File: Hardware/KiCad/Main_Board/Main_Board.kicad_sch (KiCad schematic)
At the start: 0 parts

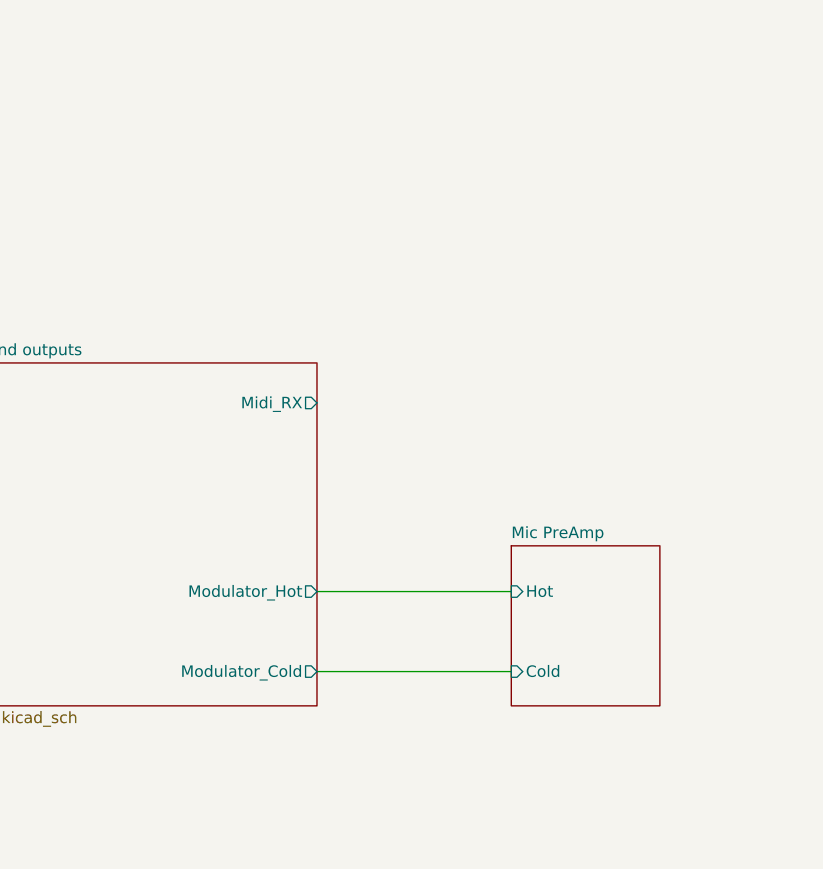
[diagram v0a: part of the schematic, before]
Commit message: Reorganised+rename Main_Board project
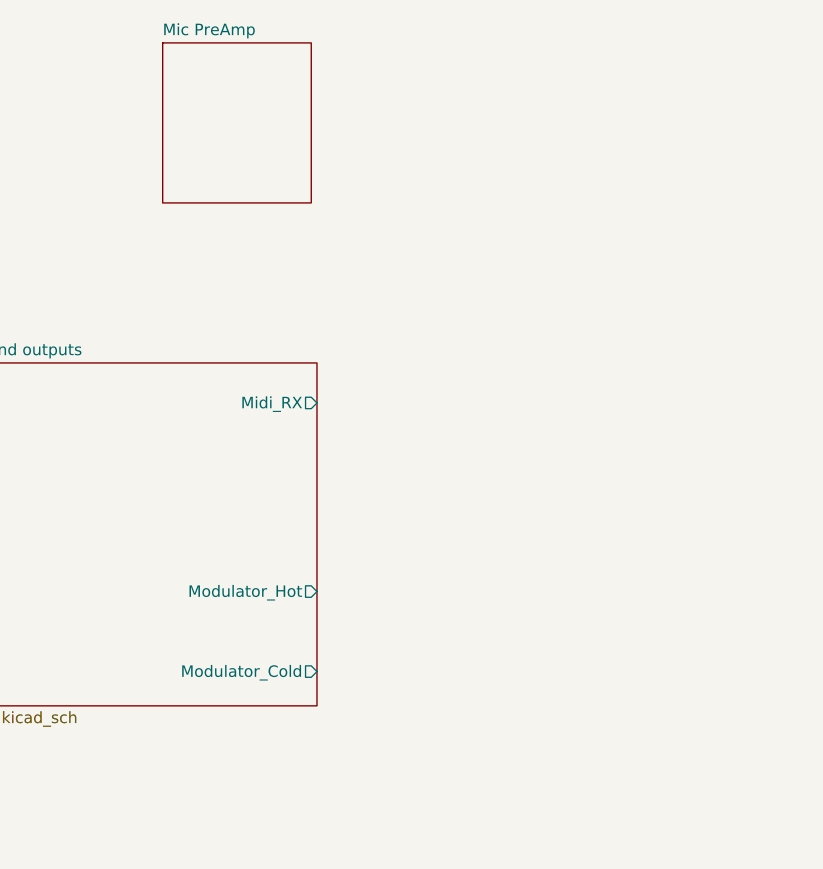
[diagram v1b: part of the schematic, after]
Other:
- sheet Mic PreAmp ports: added none; removed Cold, Hot
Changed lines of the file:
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@@
 		(comment 1 "Tim Wannet")
-	)
-	(wire
-		(pts
-			(xy 67.31 101.6) (xy 88.9 101.6)
-		)
-		(stroke
-			(width 0)
-			(type default)
-		)
-	)
-	(wire
-		(pts
-			(xy 67.31 110.49) (xy 88.9 110.49)
-		)
-		(stroke
-			(width 0)
-			(type default)
-		)
 	)
 	(sheet
@@
 		)
 		(instances
-			(project "Hardware"
+			(project "Main_Board"
 				(path "/e827c80a-ca8d-4d24-8db6-878b575a1aed"
 					(page "3")
@@
 		)
 		(instances
-			(project "Hardware"
+			(project "Main_Board"
 				(path "/e827c80a-ca8d-4d24-8db6-878b575a1aed"
 					(page "5")
@@
 		)
 		(instances
-			(project "Hardware"
+			(project "Main_Board"
 				(path "/e827c80a-ca8d-4d24-8db6-878b575a1aed"
 					(page "2")
@@
 	)
 	(sheet
-		(at 88.9 96.52)
+		(at 50.165 40.64)
 		(size 16.51 17.78)
 		(exclude_from_sim no)
@@
 		)
 		(property "Sheetname" "Mic PreAmp"
-			(at 88.9 95.8084 0)
+			(at 50.165 39.9284 0)
 			(effects
 				(font
@@
 		)
 		(property "Sheetfile" "PreAmp.kicad_sch"
-			(at 88.9 114.8846 0)
+			(at 50.165 59.0046 0)
 			(effects
 				(font
@@
 			)
 		)
-		(pin "Hot" input
-			(at 88.9 101.6 180)
-			(effects
-				(font
-					(size 1.27 1.27)
-				)
-				(justify left)
-			)
-		)
-		(pin "Cold" input
-			(at 88.9 110.49 180)
-			(effects
-				(font
-					(size 1.27 1.27)
-				)
-				(justify left)
-			)
-		)
 		(instances
-			(project "Hardware"
+			(project "Main_Board"
 				(path "/e827c80a-ca8d-4d24-8db6-878b575a1aed"
 					(page "4")

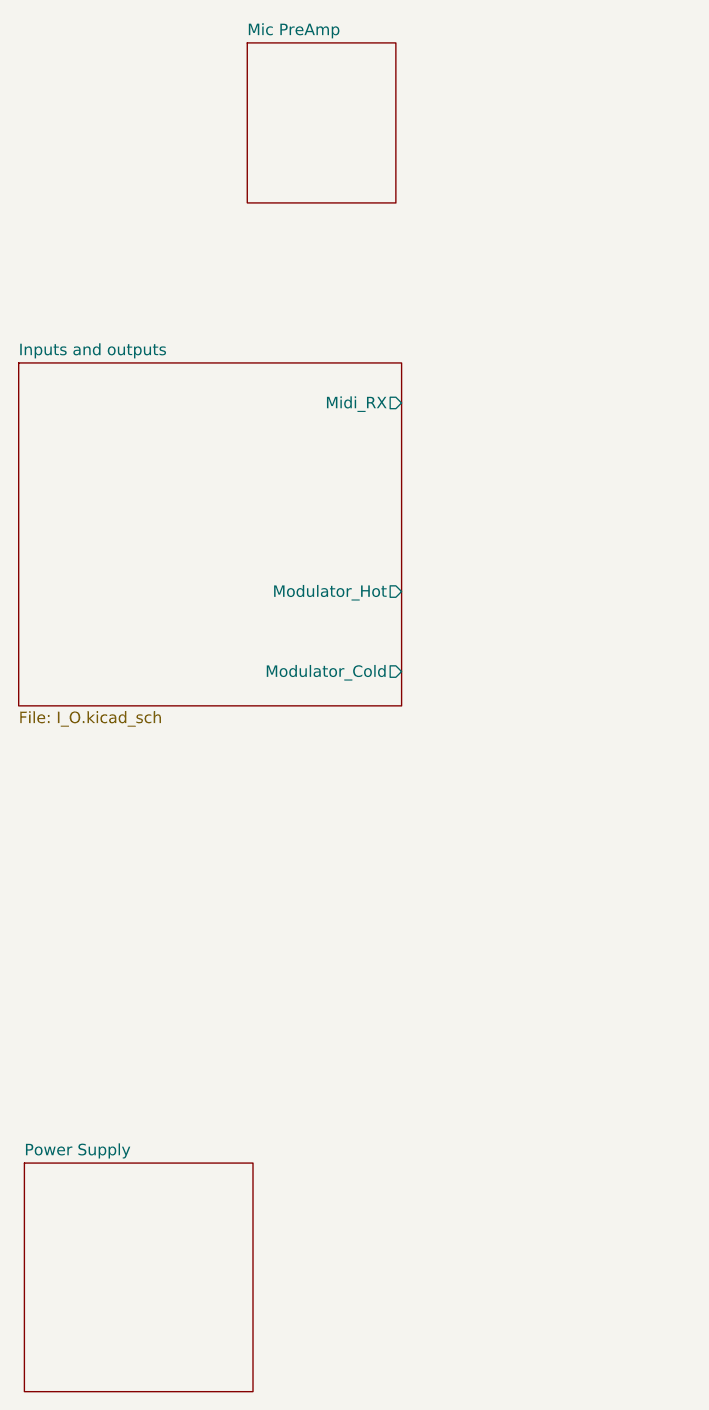
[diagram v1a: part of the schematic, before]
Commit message: Created Female header connections for MCU
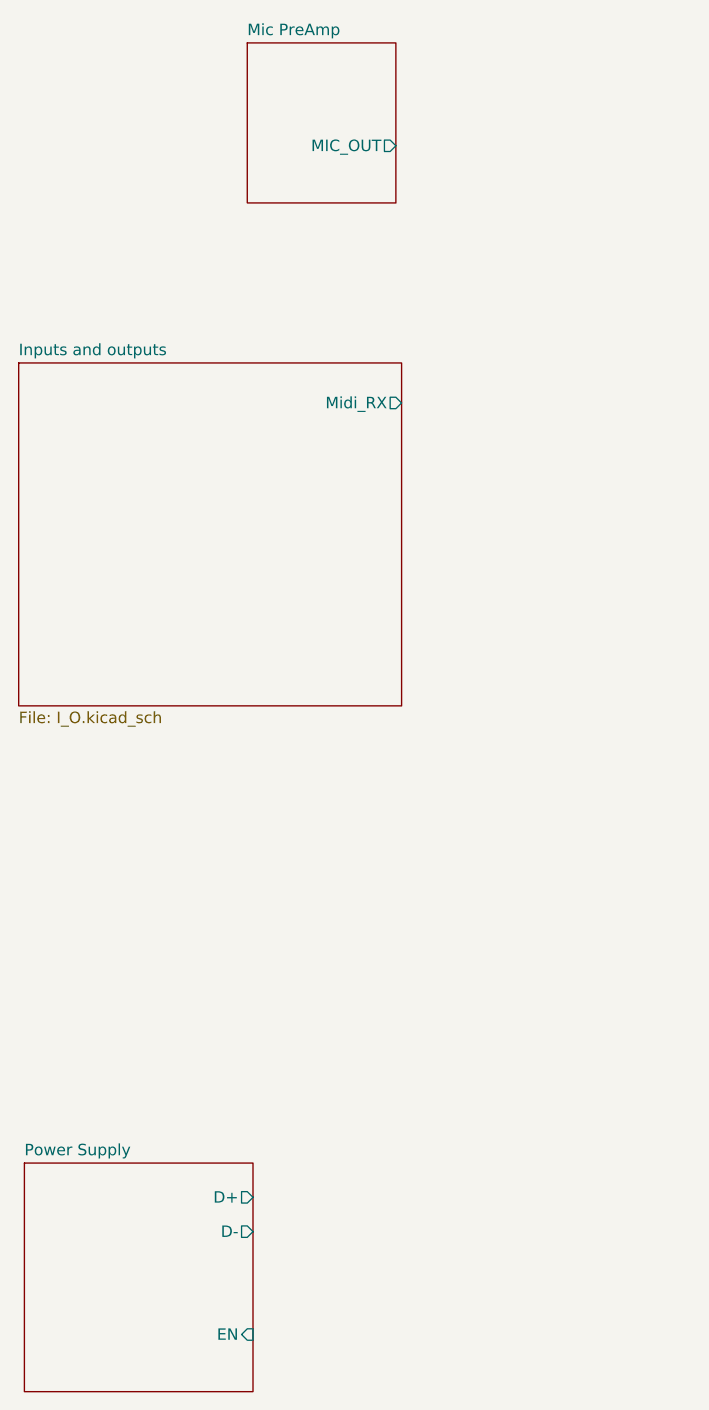
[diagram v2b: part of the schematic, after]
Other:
- sheet Inputs and outputs ports: added none; removed Modulator_Cold, Modulator_Hot
- sheet Mic PreAmp ports: added MIC_OUT; removed none
- sheet Power Supply ports: added D+, D-, EN; removed none
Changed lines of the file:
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@@
-			)
-		)
-		(pin "Modulator_Cold" output
-			(at 67.31 110.49 0)
-			(effects
-				(font
-					(size 1.27 1.27)
-				)
-				(justify right)
-			)
-		)
-		(pin "Modulator_Hot" output
-			(at 67.31 101.6 0)
-			(effects
-				(font
-					(size 1.27 1.27)
-				)
-				(justify right)
 			)
 		)
@@
 			)
 		)
+		(pin "D-" output
+			(at 50.8 172.72 0)
+			(effects
+				(font
+					(size 1.27 1.27)
+				)
+				(justify right)
+			)
+		)
+		(pin "D+" output
+			(at 50.8 168.91 0)
+			(effects
+				(font
+					(size 1.27 1.27)
+				)
+				(justify right)
+			)
+		)
+		(pin "EN" input
+			(at 50.8 184.15 0)
+			(effects
+				(font
+					(size 1.27 1.27)
+				)
+				(justify right)
+			)
+		)
 		(instances
 			(project "Main_Board"
@@
 			)
 		)
+		(pin "MIC_OUT" output
+			(at 66.675 52.07 0)
+			(effects
+				(font
+					(size 1.27 1.27)
+				)
+				(justify right)
+			)
+		)

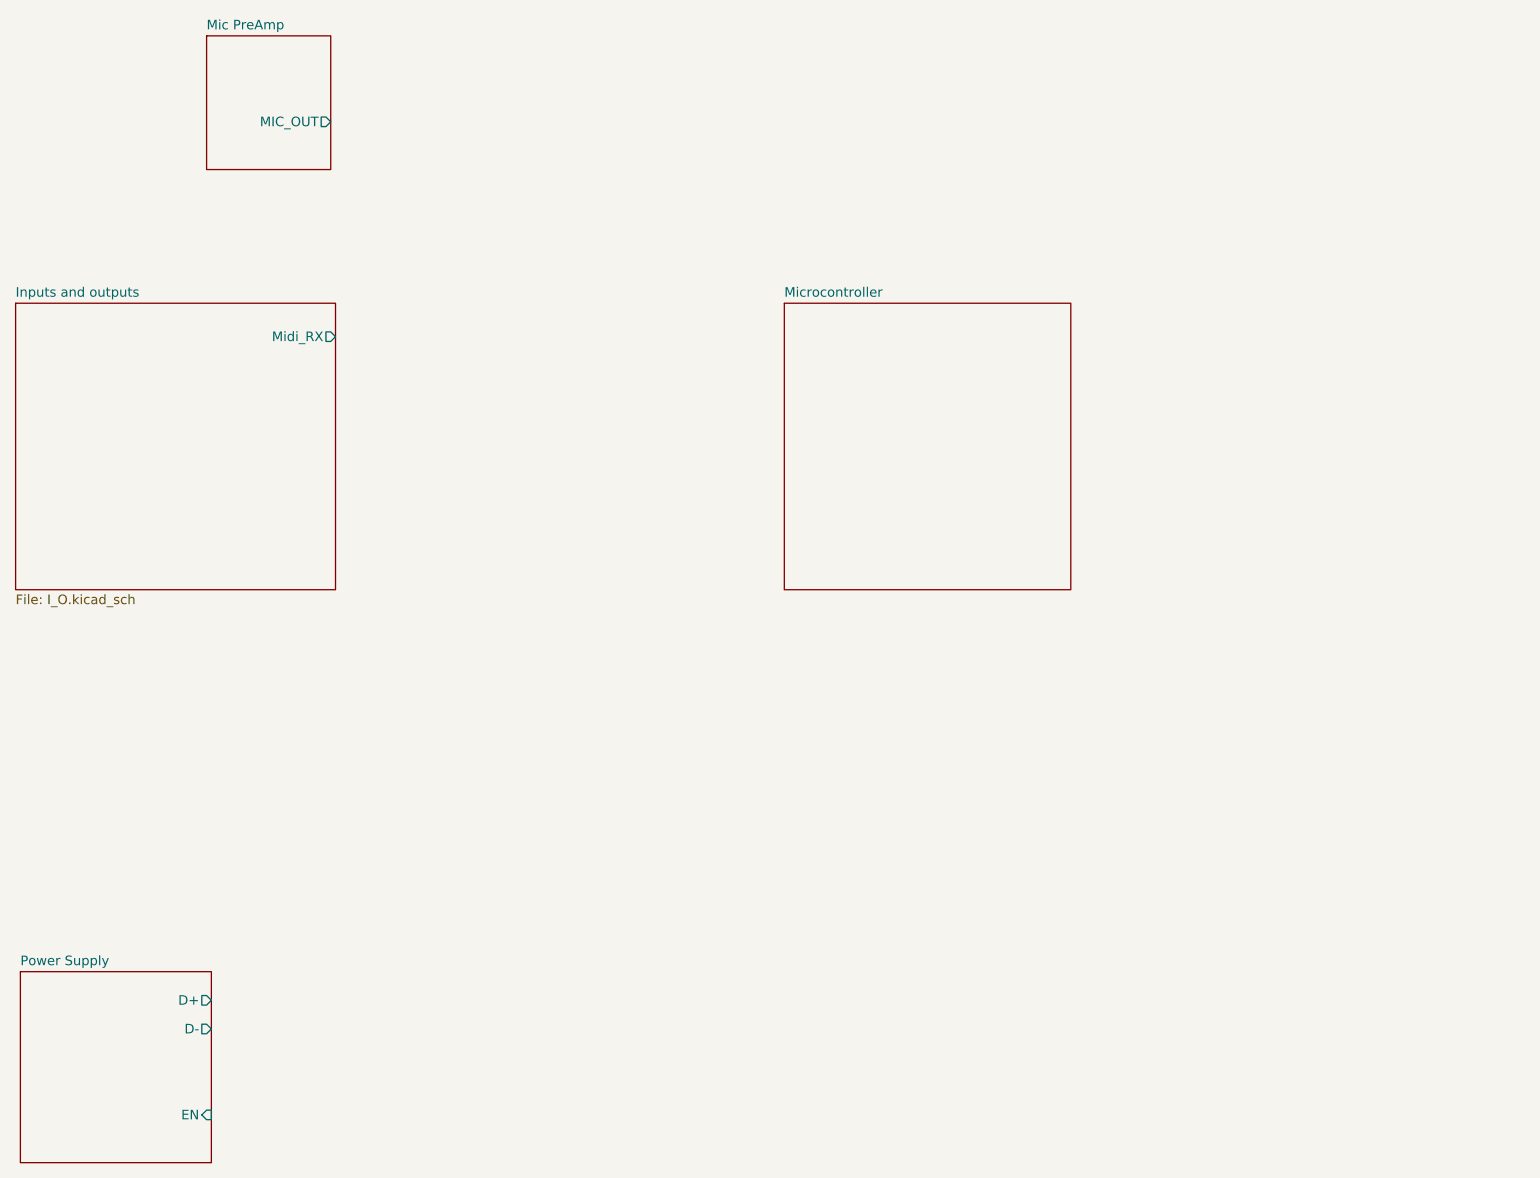
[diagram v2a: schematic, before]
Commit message: Interface hierarchical out for screen and encoder
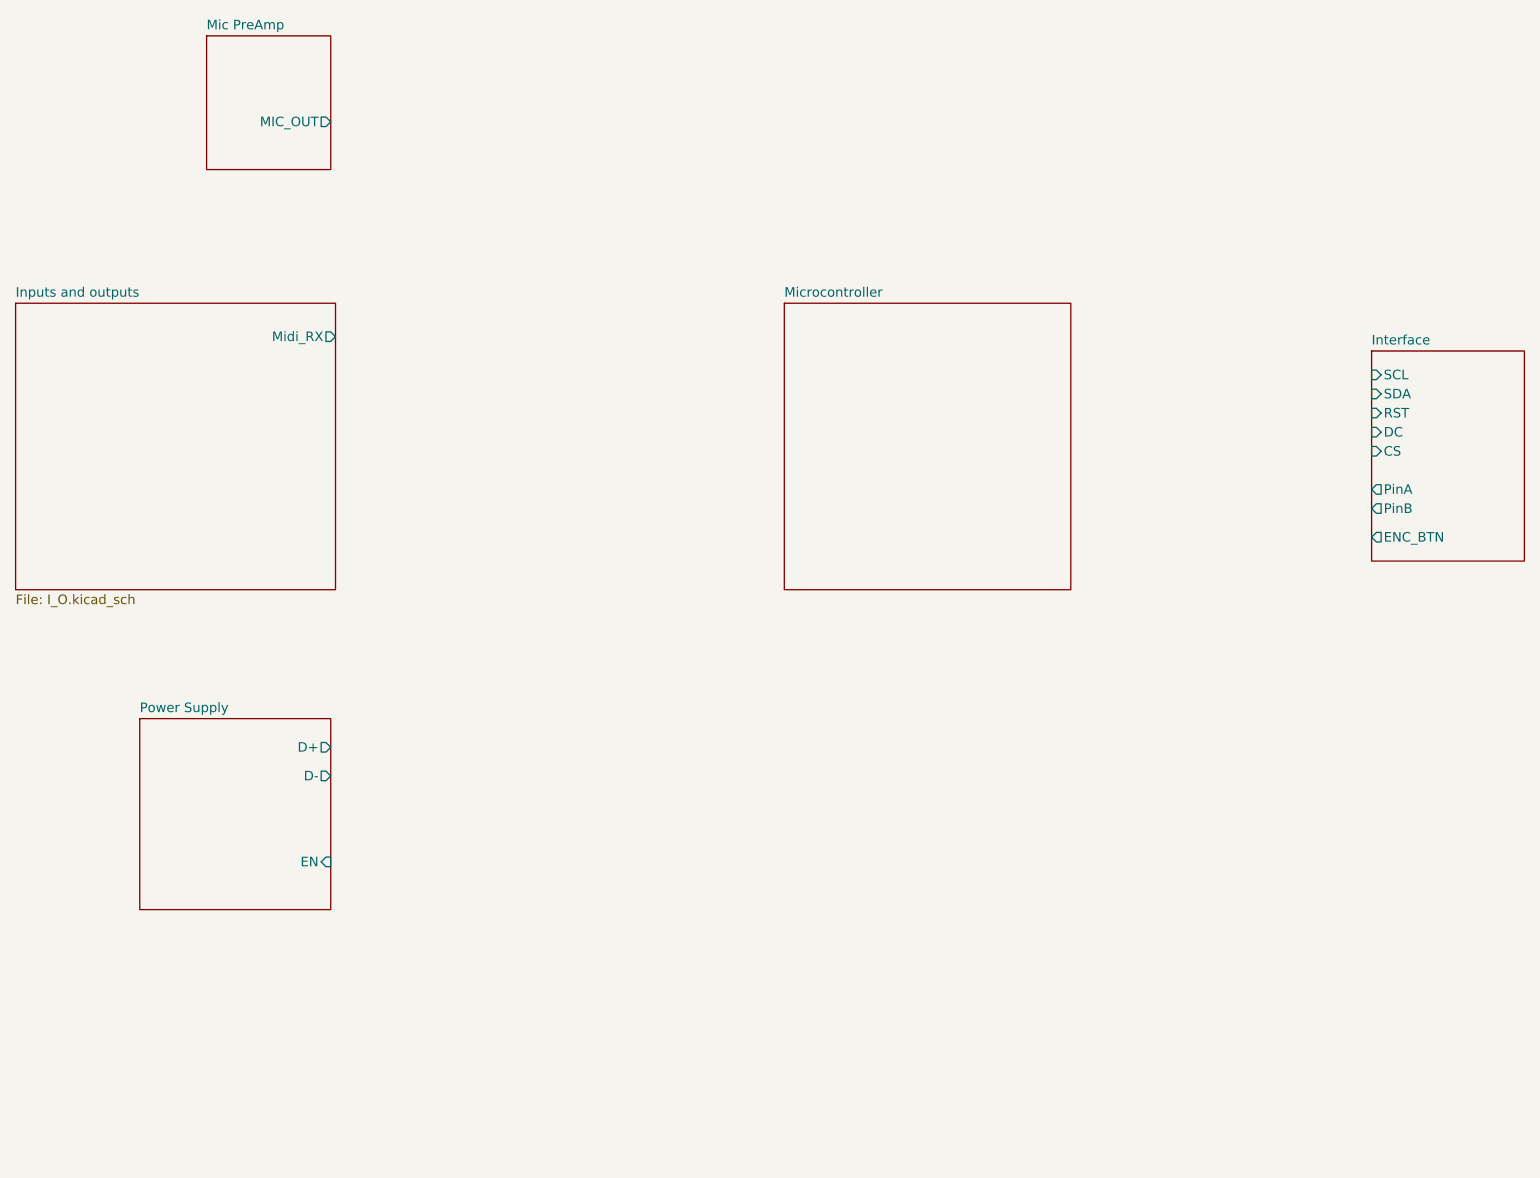
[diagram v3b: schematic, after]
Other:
- added sheet Interface (Interface.kicad_sch)
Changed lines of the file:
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@@
 	)
 	(sheet
-		(at 25.4 165.1)
+		(at 41.275 131.445)
 		(size 25.4 25.4)
 		(exclude_from_sim no)
@@
 		)
 		(property "Sheetname" "Power Supply"
-			(at 25.4 164.3884 0)
+			(at 41.275 130.7334 0)
 			(effects
 				(font
@@
 		)
 		(property "Sheetfile" "PSU.kicad_sch"
-			(at 25.4 191.0846 0)
+			(at 41.275 157.4296 0)
 			(effects
 				(font
@@
 		)
 		(pin "D-" output
-			(at 50.8 172.72 0)
+			(at 66.675 139.065 0)
 			(effects
 				(font
@@
 		)
 		(pin "D+" output
-			(at 50.8 168.91 0)
+			(at 66.675 135.255 0)
 			(effects
 				(font
@@
 		)
 		(pin "EN" input
-			(at 50.8 184.15 0)
+			(at 66.675 150.495 0)
 			(effects
 				(font
@@
 				)
 			)
+		)
+	)
+	(sheet
+		(at 205.105 82.55)
+		(size 20.32 27.94)
+		(exclude_from_sim no)
+		(in_bom yes)
+		(on_board yes)
+		(dnp no)
+		(fields_autoplaced yes)
+		(stroke
+			(width 0.1524)
+			(type solid)
+		)
+		(fill
+			(color 0 0 0 0.0000)
+		)
+		(property "Sheetname" "Interface"
+			(at 205.105 81.8384 0)
+			(effects
+				(font
+					(size 1.27 1.27)
+				)
+				(justify left bottom)
+			)
+		)
+		(property "Sheetfile" "Interface.kicad_sch"
+			(at 205.105 111.0746 0)
+			(effects
+				(font
+					(size 1.27 1.27)
+				)
+				(justify left top)
+				(hide yes)
+			)
+		)
+		(pin "CS" input
+			(at 205.105 95.885 180)
+			(effects
+				(font
+					(size 1.27 1.27)
+				)
+				(justify left)
+			)
+		)
+		(pin "SDA" input
+			(at 205.105 88.265 180)
+			(effects
+				(font
+					(size 1.27 1.27)
+				)
+				(justify left)
+			)
+		)
+		(pin "PinA" output
+			(at 205.105 100.965 180)
+			(effects
+				(font
+					(size 1.27 1.27)
+				)
+				(justify left)
+			)
+		)
+		(pin "ENC_BTN" output
+			(at 205.105 107.315 180)
+			(effects
+				(font
+					(size 1.27 1.27)
+				)
+				(justify left)
+			)
+		)
+		(pin "DC" input
+			(at 205.105 93.345 180)
+			(effects
+				(font
+					(size 1.27 1.27)
+				)
+				(justify left)
+			)
+		)
+		(pin "SCL" input
+			(at 205.105 85.725 180)
+			(effects
+				(font
+					(size 1.27 1.27)
+				)
+				(justify left)
+			)
+		)
+		(pin "PinB" output
+			(at 205.105 103.505 180)
+			(effects
+				(font
+					(size 1.27 1.27)
+				)
+				(justify left)
+			)
+		)
+		(pin "RST" input
+			(at 205.105 90.805 180)
+			(effects
+				(font
+					(size 1.27 1.27)
+				)
+				(justify left)
+			)
+		)
+		(instances
+			(project "Main_Board"
+				(path "/e827c80a-ca8d-4d24-8db6-878b575a1aed"
+					(page "6")
+				)
+			)
